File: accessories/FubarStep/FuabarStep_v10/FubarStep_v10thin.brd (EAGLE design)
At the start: 100.3 x 49.5 mm, 57 parts, among them IC1 OKI-78SR-5/1.5-W36H-C, IC2 SN754410NE, IC3 SN754410NE, X1 DC21MMX

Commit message: Updated board a bit.
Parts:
- moved C5 48.3 mm to (25.4, 3.81)
- moved C16 36.9 mm to (86.4, 44.5), turned to 90 degrees
- moved C11 34.4 mm to (118.1, 26.7)
- moved C15 31.9 mm to (113.0, 26.7)
- moved C9 14.5 mm to (80.0, 53.3)
- moved C12 13.0 mm to (88.9, 54.6)
- moved LOGO1 12.6 mm to (5.08, -6.35)
- moved C8 12.0 mm to (88.9, 12.7), turned to 270 degrees
- moved C10 11.7 mm to (64.8, 26.7)
- moved C14 10.2 mm to (68.6, 25.4)
- moved C13 9.92 mm to (91.4, 12.7)
- moved C1 7.41 mm to (27.9, 8.89), turned to 90 degrees
- moved IC3 5.68 mm to (77.5, 14.0), turned to 90 degrees
- moved IC2 5.68 mm to (77.5, 36.8), turned to 90 degrees
- moved C17 4.58 mm to (86.4, 21.6), turned to 90 degrees
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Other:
- board text added: "ANALOG INPUTS/3.3V GPIO"
- board text added: "SERVO OUTPUTS/5V GPIO"

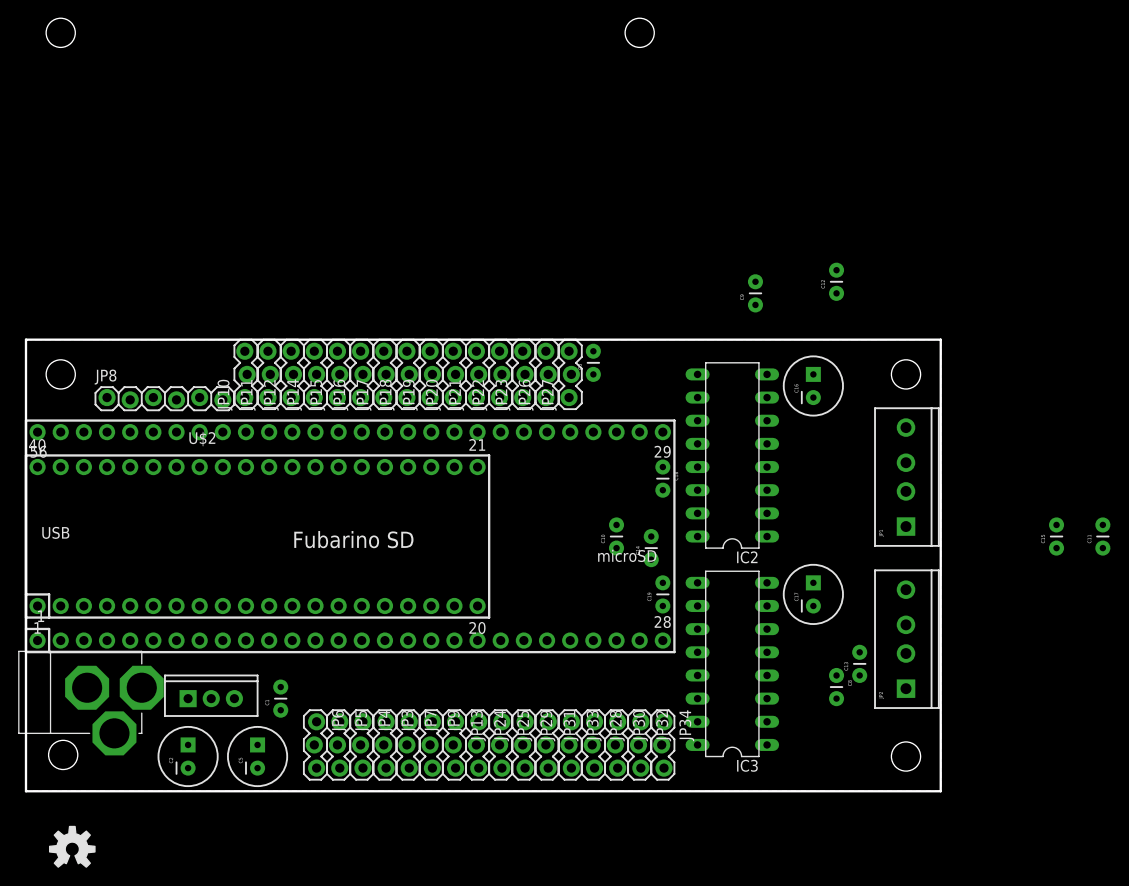
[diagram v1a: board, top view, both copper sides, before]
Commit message: Started routing. And assigned all the pins except for Mini to SD.
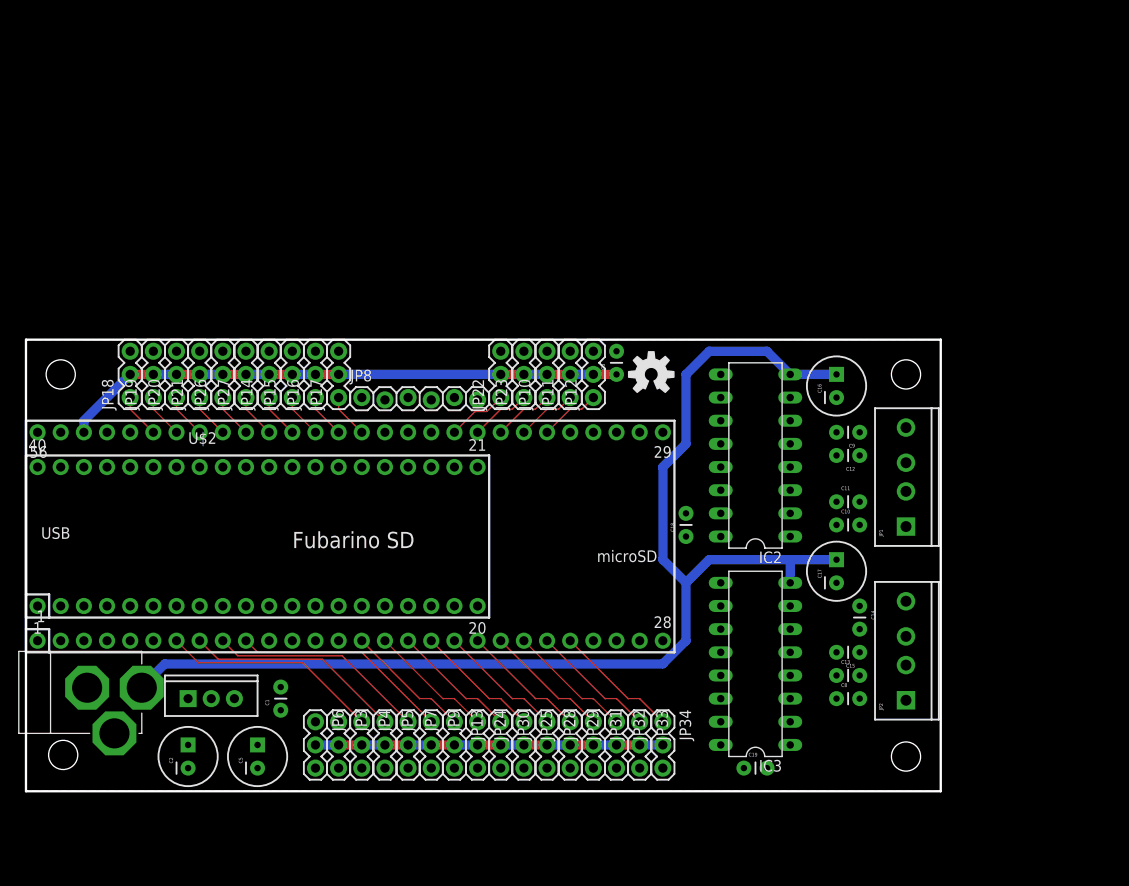
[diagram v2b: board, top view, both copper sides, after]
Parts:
- JP10, JP11, JP12, JP13, JP14, JP15, JP16, JP17, JP18, JP19, JP20, JP21, JP22, JP23, JP24, JP25, JP26, JP27, JP28, JP29, JP3, JP30, JP31, JP32, JP33, JP34, JP4, JP5, JP6, JP7, JP9: device SparkFun-Connectors:1X03_LOCK -> SparkFun-Connectors:1X03
- moved LOGO1 82.1 mm to (68.6, 45.7)
- moved JP26 35.6 mm to (21.6, 43.2)
- moved JP27 35.6 mm to (24.1, 43.2)
- moved JP10 33.0 mm to (57.1, 43.2)
- moved JP11 33.0 mm to (59.7, 43.2)
- moved JP12 33.0 mm to (62.2, 43.2)
- moved JP19 30.5 mm to (14.0, 43.2)
- moved JP20 30.5 mm to (16.5, 43.2)
- moved JP21 30.5 mm to (19.1, 43.2)
- moved JP18 30.5 mm to (11.4, 43.2)
- moved C11 29.6 mm to (88.9, 31.8), turned to 0 degrees
- moved JP8 27.9 mm to (36.8, 43.2)
- moved C15 24.4 mm to (91.4, 15.2), turned to 180 degrees
- moved C10 24.3 mm to (88.9, 29.2), turned to 0 degrees
- moved C14 23.4 mm to (91.4, 20.3), turned to 270 degrees
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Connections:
- net N$26 renamed PIN21
- net N$27 renamed PIN22
- net N$28 renamed PIN23
- net N$4 renamed PIN0
- removed net N$1: JP31.1, JP7.1
- removed net N$10: U$1.10
- removed net N$11: JP20.1
- removed net N$12: JP32.1, JP9.1
- removed net N$13: JP13.1, JP33.1
- removed net N$14: JP24.1, JP34.1
- removed net N$15: JP21.1
- removed net N$16: U$1.15
- removed net N$17: U$1.16
- removed net N$18: U$1.17
- removed net N$19: U$1.18
- removed net N$2: JP18.1
- removed net N$20: U$1.19
- removed net N$21: U$1.20
- removed net N$22: U$1.21
- removed net N$23: U$1.22
- removed net N$24: U$1.23
- removed net N$25: U$1.24
- removed net N$3: JP19.1
- removed net N$33: JP26.1
- removed net N$34: JP27.1
- removed net N$35: U$1.51
- removed net N$36: U$1.50
- removed net N$37: U$1.49
- removed net N$38: U$1.48
- removed net N$39: U$1.47
- removed net N$40: U$1.46
- removed net N$41: U$1.45
- removed net N$42: U$1.44
- removed net N$43: U$1.43
- removed net N$44: U$1.42
- removed net N$48: U$1.38
- removed net N$49: U$1.37
- removed net N$5: U$1.5
- removed net N$50: U$1.36
- removed net N$51: U$1.35
- removed net N$52: U$1.34
- removed net N$53: U$1.33
- removed net N$54: U$1.32
- removed net N$55: U$1.31
- removed net N$56: U$1.30
- removed net N$6: U$1.6
- removed net N$69: JP23.1
- removed net N$7: U$1.7
- removed net N$8: U$1.8
- removed net N$87: JP22.1
- removed net N$88: JP17.1
- removed net N$89: JP16.1
- removed net N$9: U$1.9
- removed net N$90: JP15.1
- removed net N$91: JP14.1
- removed net N$92: JP10.1
- removed net N$93: JP11.1
- removed net N$94: JP12.1
- removed net SERVO1: JP30.1, JP6.1
- removed net SERVO2: JP25.1, JP3.1
- removed net SERVO3: JP28.1, JP4.1
- removed net SERVO4: JP29.1, JP5.1
- new net A0: JP18.1, U$1.51
- new net A1: JP19.1, U$1.50
- new net A10: JP22.1, U$1.38
- new net A11: JP23.1, U$1.37
- new net A12: JP10.1, U$1.36
- new net A13: JP11.1, U$1.35
- new net A14: JP12.1, U$1.34
- new net A2: JP20.1, U$1.49
- new net A3: JP21.1, U$1.48
- new net A4: JP26.1, U$1.47
- new net A5: JP27.1, U$1.46
- new net A6: JP14.1, U$1.45
- new net A7: JP15.1, U$1.44
- new net A8: JP16.1, U$1.43
- new net A9: JP17.1, U$1.42
- new net PIN1: JP6.1, U$1.5
- new net PIN11: JP13.1, U$1.15
- new net PIN12: JP24.1, U$1.16
- new net PIN13: JP30.1, U$1.17
- new net PIN14: JP25.1, U$1.18
- new net PIN15: JP28.1, U$1.19
- new net PIN16: JP29.1, U$1.20
- new net PIN17: JP31.1, U$1.21
- new net PIN18: JP32.1, U$1.22
- new net PIN19: JP33.1, U$1.23
- new net PIN2: JP3.1, U$1.6
- new net PIN20: JP34.1, U$1.24
- new net PIN3: JP4.1, U$1.7
- new net PIN4: JP5.1, U$1.8
- new net PIN5: JP7.1, U$1.9
- new net PIN6: JP9.1, U$1.10
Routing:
- net VIN: track 0.00 -> 131.9 mm
- net 3.3V: track 0.00 -> 61.8 mm
- net +5V: track 0.00 -> 38.1 mm
- net PIN6: track 0.00 -> 24.0 mm
- net PIN5: track 0.00 -> 24.0 mm
- net PIN4: track 0.00 -> 24.0 mm
- net PIN3: track 0.00 -> 24.0 mm
- net PIN13: track 0.00 -> 13.8 mm
- net PIN12: track 0.00 -> 13.8 mm
- net PIN11: track 0.00 -> 13.8 mm
- net PIN19: track 0.00 -> 13.8 mm
- net PIN14: track 0.00 -> 13.8 mm
- net PIN20: track 0.00 -> 13.8 mm
- net PIN18: track 0.00 -> 13.8 mm
- net PIN17: track 0.00 -> 13.8 mm
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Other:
- board text added: "FTDI"

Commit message: More routing.
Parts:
- removed JP3, JP4, JP5, JP6: (no value), SparkFun-Connectors:1X03
- moved C1 4.58 mm to (30.5, 5.08), turned to 270 degrees
- moved JP33 2.84 mm to (64.8, 6.35)
- moved JP9 2.84 mm to (41.9, 6.35)
- moved JP13 2.84 mm to (44.5, 6.35)
- moved JP24 2.84 mm to (47.0, 6.35)
- moved JP25 2.84 mm to (52.1, 6.35)
- moved JP28 2.84 mm to (54.6, 6.35)
- moved JP29 2.84 mm to (57.1, 6.35)
- moved JP30 2.84 mm to (49.5, 6.35)
- moved JP31 2.84 mm to (59.7, 6.35)
- moved JP32 2.84 mm to (62.2, 6.35)
- moved JP7 2.84 mm to (39.4, 6.35)
- moved JP34 2.84 mm to (67.3, 6.35)
- moved C18 2.54 mm to (69.8, 27.9), turned to 270 degrees
- moved C8 2.54 mm to (88.9, 7.62)
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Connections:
- removed net PIN0: U$1.4
- removed net PIN1: JP6.1, U$1.5
- removed net PIN11: JP13.1, U$1.15
- removed net PIN2: JP3.1, U$1.6
- removed net PIN3: JP4.1, U$1.7
- removed net PIN4: JP5.1, U$1.8
- removed net PIN5: JP7.1, U$1.9
- removed net PIN6: JP9.1, U$1.10
- net +5V: no longer JP3.2, JP4.2, JP5.2, JP6.2
- net GND: no longer JP3.3, JP4.3, JP5.3, JP6.3
- net M1A1: now also U$1.4
- net M1A2: now also U$1.5
- net M1A3: now also U$1.6
- net M1A4: now also U$1.7
- net M2A1: now also U$1.10
- net M2A2: now also U$1.15, U$1.9
- net M2A3: now also U$1.8
- net PIN12: now also JP7.1; no longer JP24.1
- net PIN13: now also JP9.1; no longer JP30.1
- net PIN14: now also JP13.1; no longer JP25.1
- net PIN15: now also JP24.1; no longer JP28.1
- net PIN16: now also JP30.1; no longer JP29.1
- net PIN17: now also JP25.1; no longer JP31.1
- net PIN18: now also JP28.1; no longer JP32.1
- net PIN19: now also JP29.1; no longer JP33.1
- net PIN20: now also JP31.1; no longer JP34.1
- net PIN21: now also JP32.1
- net PIN22: now also JP33.1
- net PIN23: now also JP34.1
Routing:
- net +5V: track 38.1 -> 138.5 mm, vias 0 -> 2
- net M2EN12: track 0.00 -> 56.7 mm
- net M2A1: track 0.00 -> 53.6 mm
- net M2A2: track 0.00 -> 51.4 mm, vias 0 -> 2
- net M2A3: track 0.00 -> 49.2 mm, vias 0 -> 1
- net M2EN34: track 0.00 -> 48.3 mm, vias 0 -> 1
- net M2A4: track 0.00 -> 46.8 mm
- net M1A2: track 0.00 -> 44.0 mm, vias 0 -> 2
- net M1O4: track 0.00 -> 38.4 mm
- net TX: track 0.00 -> 37.8 mm
- net M2O4: track 0.00 -> 37.4 mm
- net RX: track 0.00 -> 37.1 mm
- net M1A3: track 0.00 -> 36.2 mm, vias 0 -> 1
- net M1EN34: track 0.00 -> 31.5 mm, vias 0 -> 1
- net M1A1: track 0.00 -> 29.9 mm, vias 0 -> 2
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
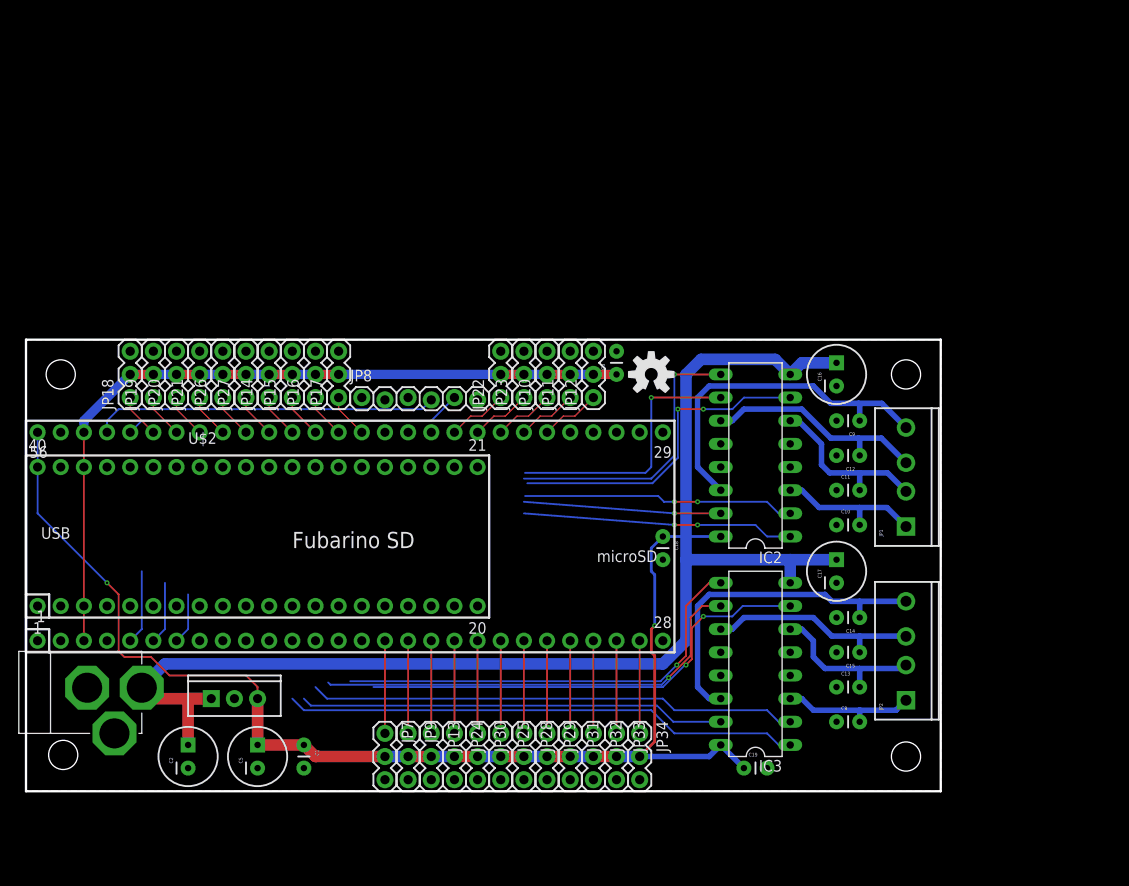
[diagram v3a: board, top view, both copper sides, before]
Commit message: Routing is done, but Mini connections not yet made. Top silk is almost done.
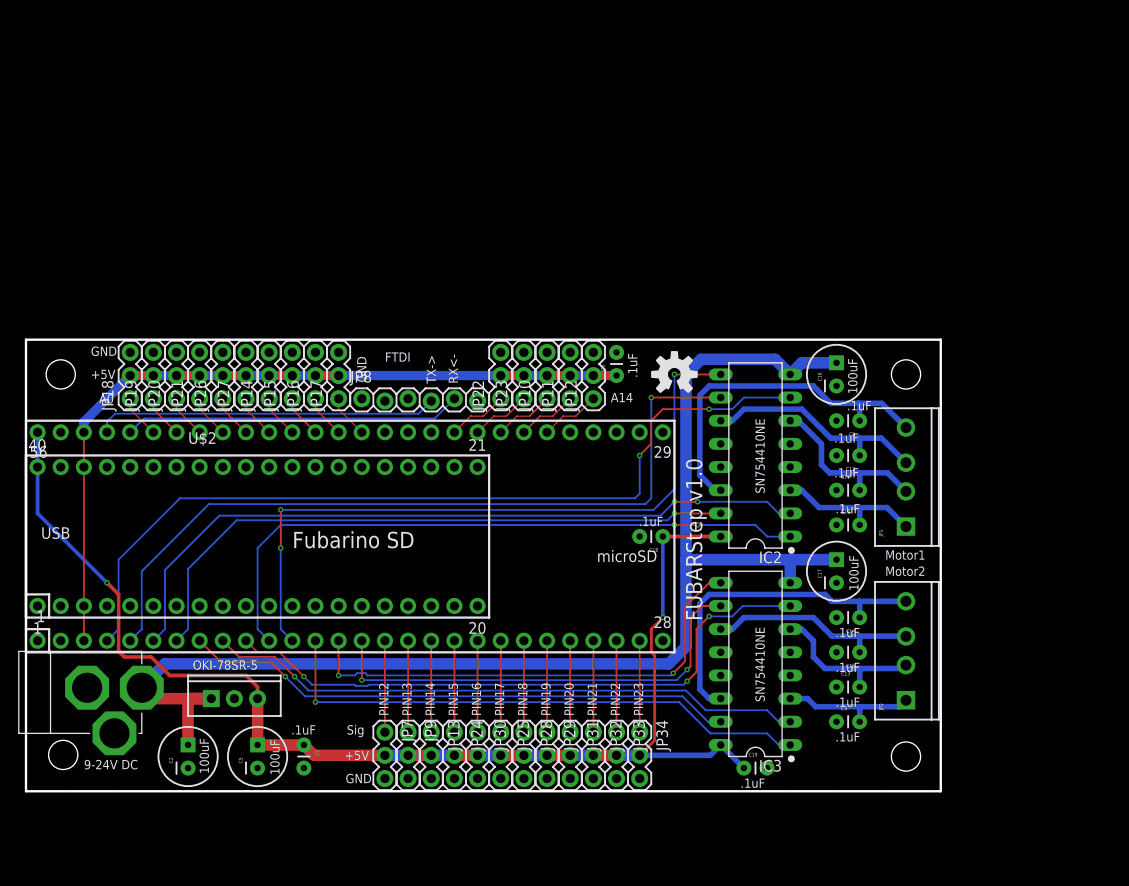
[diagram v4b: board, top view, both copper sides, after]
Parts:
- moved LOGO1 2.54 mm to (71.1, 45.7)
- moved JP10 0.13 mm to (57.1, 43.1)
- moved JP11 0.13 mm to (59.7, 43.1)
- moved JP12 0.13 mm to (62.2, 43.1)
- moved JP14 0.13 mm to (26.7, 43.1)
- moved JP15 0.13 mm to (29.2, 43.1)
- moved JP16 0.13 mm to (31.8, 43.1)
- moved JP17 0.13 mm to (34.3, 43.1)
- moved JP18 0.13 mm to (11.4, 43.1)
- moved JP19 0.13 mm to (14.0, 43.1)
- moved JP20 0.13 mm to (16.5, 43.1)
- moved JP21 0.13 mm to (19.1, 43.1)
- moved JP22 0.13 mm to (52.1, 43.1)
- moved JP23 0.13 mm to (54.6, 43.1)
- moved JP26 0.13 mm to (21.6, 43.1)
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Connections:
- removed net N$59: U$2.28
- removed net N$60: U$2.27
- removed net N$61: U$2.26
- removed net N$62: U$2.25
- removed net N$63: U$2.24
- removed net N$64: U$2.23
- removed net N$65: U$2.22
- removed net N$66: U$2.21
- removed net N$70: U$2.4
- removed net N$71: U$2.5
- removed net N$72: U$2.6
- removed net N$73: U$2.7
- removed net N$74: U$2.8
- removed net N$75: U$2.9
- removed net N$76: U$2.10
- removed net N$77: U$2.11
- removed net N$78: U$2.12
- removed net N$79: U$2.13
- removed net N$80: U$2.14
- removed net N$81: U$2.15
- removed net N$82: U$2.16
- removed net N$83: U$2.17
- removed net N$84: U$2.18
- removed net N$85: U$2.19
- removed net N$86: U$2.20
- net A10: now also U$2.16
- net A11: now also U$2.17
- net A12: now also U$2.24
- net M1A1: now also U$1.6, U$2.6; no longer U$1.4
- net M1A2: now also U$1.4, U$2.4; no longer U$1.5
- net M1A3: now also U$1.5, U$2.5; no longer U$1.6
- net M1A4: now also U$2.7
- net M1EN12: now also U$2.11
- net M1EN34: now also U$2.12
- net M2A1: now also U$1.9, U$2.9; no longer U$1.10
- net M2A2: now also U$1.10, U$2.10; no longer U$1.15, U$1.9
- net M2A3: now also U$1.15, U$2.15; no longer U$1.8
- net M2A4: now also U$1.8, U$2.8
- net M2EN12: now also U$2.13
- net M2EN34: now also U$2.14
- net PIN14: now also U$2.18
- net PIN15: now also U$2.19
- net PIN16: now also U$2.20
- net PIN17: now also U$2.28
- net PIN18: now also U$2.27
- net PIN19: now also U$2.26
- net PIN20: now also U$2.25
- net PIN21: now also U$2.23
- net PIN22: now also U$2.22
- net PIN23: now also U$2.21
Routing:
- net M1A1: track 29.9 -> 80.5 mm
- net M1A2: track 44.0 -> 94.4 mm
- net M1A3: track 36.2 -> 86.0 mm
- net M1EN34: track 31.5 -> 76.7 mm, vias 1 -> 3
- net M1A4: track 27.2 -> 69.3 mm
- net M1EN12: track 29.8 -> 70.7 mm
- net M2A2: track 51.4 -> 68.1 mm, vias 2 -> 3
- net M2A4: track 46.8 -> 60.8 mm, vias 0 -> 1
- net M2A1: track 53.6 -> 65.9 mm, vias 0 -> 1
- net M2EN34: track 48.3 -> 53.6 mm, vias 1 -> 2
- net M2EN12: track 56.7 -> 60.7 mm, vias 0 -> 1
- net M2A3: track 49.2 -> 50.2 mm, vias 1 -> 2
- net +5V: track 138.5 -> 138.0 mm
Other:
- board text added: "+5V"
- board text added: ".1uF"
- board text added: "100uF"
- board text added: "9-24V DC"
- board text added: "A0"
- board text added: "A14"
- board text added: "FUBARStep v1.0"
- board text added: "GND"
- board text added: "Motor1"
- board text added: "Motor2"
- board text added: "OKI-78SR-5"
- board text added: "PIN12"
- board text added: "PIN13"
- board text added: "PIN14"
- board text added: "PIN15"
- board text added: "PIN16"
- board text added: "PIN17"
- board text added: "PIN18"
- board text added: "PIN19"
- board text added: "PIN20"
- board text added: "PIN21"
- board text added: "PIN22"
- board text added: "PIN23"
- board text added: "RX<-"
- board text added: "SN754410NE"
- board text added: "Sig"
- board text added: "TX->"
